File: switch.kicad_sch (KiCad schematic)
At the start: 2 parts, among them SW2 SW_Nidec_CAS-120A1

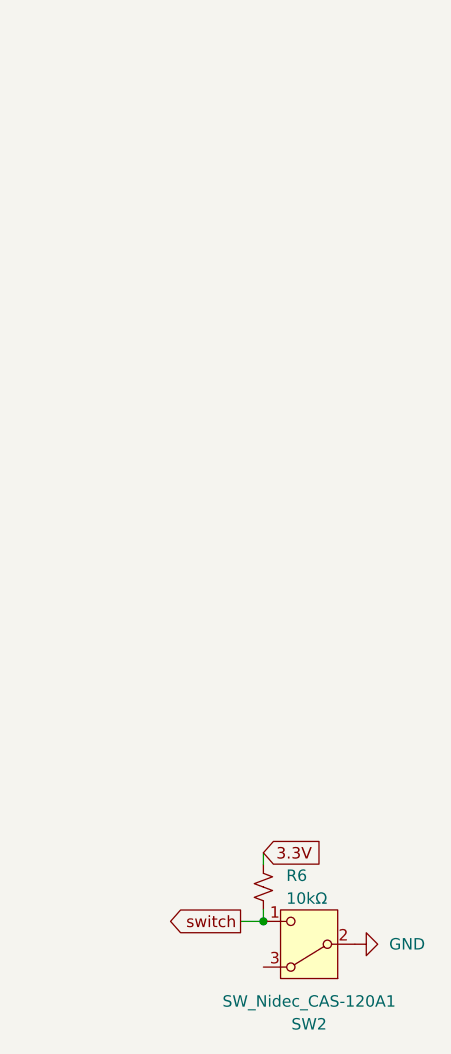
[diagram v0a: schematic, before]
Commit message: Overhaul
Overhauled the schematic so all the components are correct, rewired power to be 12 V instead of 9 V and connected hierarchical labels between modules. Added more decoupling capacitors where they were missing.
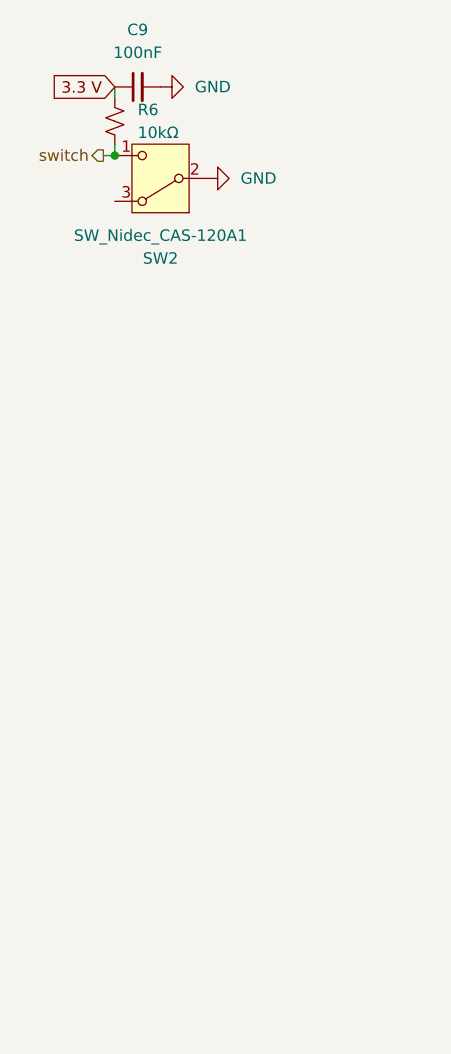
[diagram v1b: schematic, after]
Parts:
- added C9: 100nF, symbol Device:C_Small
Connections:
- net GND: now also C9.2
- net 3.3V renamed 3.3 V
- net 3.3 V: now also C9.1
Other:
- moved on the sheet: R6, SW2
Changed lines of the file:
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@@
 	(paper "A4")
 	(junction
-		(at 46.99 116.84)
+		(at 30.48 31.75)
 		(diameter 0)
 		(color 0 0 0 0)
@@
 	(wire
 		(pts
-			(xy 46.99 109.22) (xy 46.99 110.49)
+			(xy 30.48 24.13) (xy 30.48 25.4)
 		)
 		(stroke
@@
 	(wire
 		(pts
-			(xy 44.45 116.84) (xy 46.99 116.84)
+			(xy 29.21 31.75) (xy 30.48 31.75)
 		)
 		(stroke
@@
 	(wire
 		(pts
-			(xy 46.99 115.57) (xy 46.99 116.84)
+			(xy 30.48 30.48) (xy 30.48 31.75)
 		)
 		(stroke
@@
 		)
 	)
-	(global_label "switch"
-		(shape output)
-		(at 44.45 116.84 180)
+	(global_label "3.3 V"
+		(shape input)
+		(at 30.48 24.13 180)
 		(fields_autoplaced yes)
 		(effects
@@
 		)
 		(property "Intersheetrefs" "${INTERSHEET_REFS}"
-			(at 35.5381 116.84 0)
+			(at 22.4148 24.13 0)
 			(hide yes)
 			(show_name no)
@@
 		)
 	)
-	(global_label "3.3V"
-		(shape input)
-		(at 46.99 109.22 0)
-		(fields_autoplaced yes)
+	(hierarchical_label "switch"
+		(shape output)
+		(at 29.21 31.75 180)
 		(effects
 			(font
 				(size 1.27 1.27)
 			)
-			(justify left)
-		)
-		(property "Intersheetrefs" "${INTERSHEET_REFS}"
-			(at 54.0876 109.22 0)
-			(hide yes)
-			(show_name no)
-			(do_not_autoplace no)
-			(effects
-				(font
-					(size 1.27 1.27)
-				)
-				(justify left)
-			)
+			(justify right)
 		)
 	)
 	(symbol
 		(lib_id "Switch:SW_Nidec_CAS-120A1")
-		(at 52.07 119.38 180)
+		(at 35.56 34.29 180)
 		(unit 1)
 		(body_style 1)
@@
 		(fields_autoplaced yes)
 		(property "Reference" "SW2"
-			(at 52.07 128.27 0)
+			(at 35.56 43.18 0)
 			(show_name no)
 			(do_not_autoplace no)
@@
 		)
 		(property "Value" "SW_Nidec_CAS-120A1"
-			(at 52.07 125.73 0)
+			(at 35.56 40.64 0)
 			(show_name no)
 			(do_not_autoplace no)
@@
 		)
 		(property "Footprint" "Button_Switch_SMD:Nidec_Copal_CAS-120A"
-			(at 52.07 109.22 0)
+			(at 35.56 24.13 0)
 			(hide yes)
 			(show_name no)
@@
 		)
 		(property "Datasheet" "https://www.nidec-components.com/e/catalog/switch/cas.pdf"
-			(at 52.07 111.76 0)
+			(at 35.56 26.67 0)
 			(hide yes)
 			(show_name no)
@@
 		)
 		(property "Description" "Switch, single pole double throw"
-			(at 52.07 119.38 0)
+			(at 35.56 34.29 0)
 			(hide yes)
 			(show_name no)
@@
 	(symbol
 		(lib_id "power:GND")
-		(at 57.15 119.38 90)
+		(at 35.56 24.13 90)
 		(unit 1)
 		(body_style 1)
@@
 		(dnp no)
 		(fields_autoplaced yes)
-		(property "Reference" "#PWR014"
-			(at 63.5 119.38 0)
+		(property "Reference" "#PWR08"
+			(at 41.91 24.13 0)
 			(hide yes)
 			(show_name no)
@@
 		)
 		(property "Value" "GND"
-			(at 60.96 119.3799 90)
+			(at 39.37 24.1299 90)
 			(show_name no)
 			(do_not_autoplace no)
@@
 		)
 		(property "Footprint" ""
-			(at 57.15 119.38 0)
+			(at 35.56 24.13 0)
 			(hide yes)
 			(show_name no)
@@
 		)
 		(property "Datasheet" ""
-			(at 57.15 119.38 0)
+			(at 35.56 24.13 0)
 			(hide yes)
 			(show_name no)
@@
 		)
 		(property "Description" "Power symbol creates a global label with name \"GND\" , ground"
-			(at 57.15 119.38 0)
+			(at 35.56 24.13 0)
 			(hide yes)
 			(show_name no)
@@
 			(project "X19-Float-Board"
 				(path "/00000000-0000-0000-0000-000060e6118b/0ac88440-db6d-4d31-a4a6-0df1c7290ceb"
-					(reference "#PWR014")
+					(reference "#PWR08")
 					(unit 1)
 				)
@@
 	)
 	(symbol
-		(lib_id "Device:R_Small_US")
-		(at 46.99 113.03 180)
+		(lib_id "Device:C_Small")
+		(at 33.02 24.13 90)
 		(unit 1)
 		(body_style 1)
@@
 		(dnp no)
 		(fields_autoplaced yes)
+		(property "Reference" "C9"
+			(at 33.0263 17.78 90)
+			(show_name no)
+			(do_not_autoplace no)
+			(effects
+				(font
+					(size 1.27 1.27)
+				)
+			)
+		)
+		(property "Value" "100nF"
+			(at 33.0263 20.32 90)
+			(show_name no)
+			(do_not_autoplace no)
+			(effects
+				(font
+					(size 1.27 1.27)
+				)
+			)
+		)
+		(property "Footprint" ""
+			(at 33.02 24.13 0)
+			(hide yes)
+			(show_name no)
+			(do_not_autoplace no)
+			(effects
+				(font
+					(size 1.27 1.27)
+				)
+			)
+		)
+		(property "Datasheet" ""
+			(at 33.02 24.13 0)
+			(hide yes)
+			(show_name no)
+			(do_not_autoplace no)
+			(effects
+				(font
+					(size 1.27 1.27)
+				)
+			)
+		)
+		(property "Description" "Unpolarized capacitor, small symbol"
+			(at 33.02 24.13 0)
+			(hide yes)
+			(show_name no)
+			(do_not_autoplace no)
+			(effects
+				(font
+					(size 1.27 1.27)
+				)
+			)
+		)
+		(pin "1"
+		)
+		(pin "2"
+		)
+		(instances
+			(project "X19-Float-Board"
+				(path "/00000000-0000-0000-0000-000060e6118b/0ac88440-db6d-4d31-a4a6-0df1c7290ceb"
+					(reference "C9")
+					(unit 1)
+				)
+			)
+		)
+	)
+	(symbol
+		(lib_id "power:GND")
+		(at 40.64 34.29 90)
+		(unit 1)
+		(body_style 1)
+		(exclude_from_sim no)
+		(in_bom yes)
+		(on_board yes)
+		(in_pos_files yes)
+		(dnp no)
+		(fields_autoplaced yes)
+		(property "Reference" "#PWR014"
+			(at 46.99 34.29 0)
+			(hide yes)
+			(show_name no)
+			(do_not_autoplace no)
+			(effects
+				(font
+					(size 1.27 1.27)
+				)
+			)
+		)
+		(property "Value" "GND"
+			(at 44.45 34.2899 90)
+			(show_name no)
+			(do_not_autoplace no)
+			(effects
+				(font
+					(size 1.27 1.27)
+				)
+				(justify right)
+			)
+		)
+		(property "Footprint" ""
+			(at 40.64 34.29 0)
+			(hide yes)
+			(show_name no)
+			(do_not_autoplace no)
+			(effects
+				(font
+					(size 1.27 1.27)
+				)
+			)
+		)
+		(property "Datasheet" ""
+			(at 40.64 34.29 0)
+			(hide yes)
+			(show_name no)
+			(do_not_autoplace no)
+			(effects
+				(font
+					(size 1.27 1.27)
+				)
+			)
+		)
+		(property "Description" "Power symbol creates a global label with name \"GND\" , ground"
+			(at 40.64 34.29 0)
+			(hide yes)
+			(show_name no)
+			(do_not_autoplace no)
+			(effects
+				(font
+					(size 1.27 1.27)
+				)
+			)
+		)
+		(pin "1"
+		)
+		(instances
+			(project "X19-Float-Board"
+				(path "/00000000-0000-0000-0000-000060e6118b/0ac88440-db6d-4d31-a4a6-0df1c7290ceb"
+					(reference "#PWR014")
+					(unit 1)
+				)
+			)
+		)
+	)
+	(symbol
+		(lib_id "Device:R_Small_US")
+		(at 30.48 27.94 180)
+		(unit 1)
+		(body_style 1)
+		(exclude_from_sim no)
+		(in_bom yes)
+		(on_board yes)
+		(in_pos_files yes)
+		(dnp no)
+		(fields_autoplaced yes)
 		(property "Reference" "R6"
-			(at 49.53 111.7599 0)
+			(at 33.02 26.6699 0)
 			(show_name no)
 			(do_not_autoplace no)
@@
 		)
 		(property "Value" "10kΩ"
-			(at 49.53 114.2999 0)
+			(at 33.02 29.2099 0)
 			(show_name no)
 			(do_not_autoplace no)
@@
 		)
 		(property "Footprint" ""
-			(at 46.99 113.03 0)
+			(at 30.48 27.94 0)
 			(hide yes)
 			(show_name no)
@@
 		)
 		(property "Datasheet" ""
-			(at 46.99 113.03 0)
+			(at 30.48 27.94 0)
 			(hide yes)
 			(show_name no)
@@
 		)
 		(property "Description" "Resistor, small US symbol"
-			(at 46.99 113.03 0)
-			(hide yes)
-			(show_name no)
+			(at 30.48 27.94 0)
+			(hide yes)
+			(show_name no)

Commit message: Gave footprints to everything
Footprints
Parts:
- C9: footprint (none) -> Capacitor_SMD:C_0603_1608Metric
- R6: footprint (none) -> Resistor_SMD:R_0603_1608Metric
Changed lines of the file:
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@@
 			)
 		)
-		(property "Footprint" ""
+		(property "Footprint" "Capacitor_SMD:C_0603_1608Metric"
 			(at 33.02 24.13 0)
 			(hide yes)
@@
 			)
 		)
-		(property "Footprint" ""
+		(property "Footprint" "Resistor_SMD:R_0603_1608Metric"
 			(at 30.48 27.94 0)
 			(hide yes)

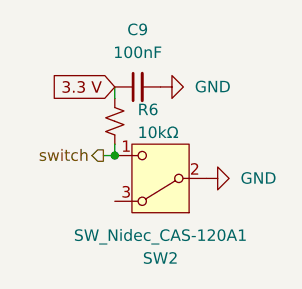
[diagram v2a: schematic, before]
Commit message: USB-C + Complete wiring
Compltetly wired the pcb (I don't understand the DRC errors) and added a usb C to flash the stm, modified the switch to be the BOOT0 for the stm so it controls whether the stm is in flash mode
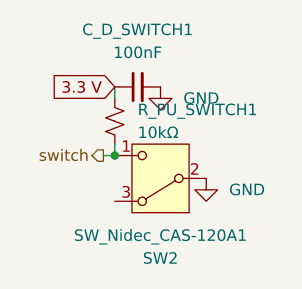
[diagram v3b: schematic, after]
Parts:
- renumbered C9 to C_D_SWITCH1, R6 to R_PU_SWITCH1
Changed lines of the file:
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@@
 	(symbol
 		(lib_id "power:GND")
-		(at 35.56 24.13 90)
+		(at 35.56 24.13 0)
 		(unit 1)
 		(body_style 1)
@@
 		(fields_autoplaced yes)
 		(property "Reference" "#PWR08"
-			(at 41.91 24.13 0)
+			(at 35.56 30.48 0)
 			(hide yes)
 			(show_name no)
@@
 		)
 		(property "Value" "GND"
-			(at 39.37 24.1299 90)
-			(show_name no)
-			(do_not_autoplace no)
-			(effects
-				(font
-					(size 1.27 1.27)
-				)
-				(justify right)
+			(at 38.1 25.3999 0)
+			(show_name no)
+			(do_not_autoplace no)
+			(effects
+				(font
+					(size 1.27 1.27)
+				)
+				(justify left)
 			)
 		)
@@
 		(dnp no)
 		(fields_autoplaced yes)
-		(property "Reference" "C9"
+		(property "Reference" "C_D_SWITCH1"
 			(at 33.0263 17.78 90)
 			(show_name no)
@@
 			(project "X19-Float-Board"
 				(path "/00000000-0000-0000-0000-000060e6118b/0ac88440-db6d-4d31-a4a6-0df1c7290ceb"
-					(reference "C9")
+					(reference "C_D_SWITCH1")
 					(unit 1)
 				)
@@
 	(symbol
 		(lib_id "power:GND")
-		(at 40.64 34.29 90)
+		(at 40.64 34.29 0)
 		(unit 1)
 		(body_style 1)
@@
 		(fields_autoplaced yes)
 		(property "Reference" "#PWR014"
-			(at 46.99 34.29 0)
+			(at 40.64 40.64 0)
 			(hide yes)
 			(show_name no)
@@
 		)
 		(property "Value" "GND"
-			(at 44.45 34.2899 90)
-			(show_name no)
-			(do_not_autoplace no)
-			(effects
-				(font
-					(size 1.27 1.27)
-				)
-				(justify right)
+			(at 43.18 35.5599 0)
+			(show_name no)
+			(do_not_autoplace no)
+			(effects
+				(font
+					(size 1.27 1.27)
+				)
+				(justify left)
 			)
 		)
@@
 		(dnp no)
 		(fields_autoplaced yes)
-		(property "Reference" "R6"
+		(property "Reference" "R_PU_SWITCH1"
 			(at 33.02 26.6699 0)
 			(show_name no)
@@
 			(project "X19-Float-Board"
 				(path "/00000000-0000-0000-0000-000060e6118b/0ac88440-db6d-4d31-a4a6-0df1c7290ceb"
-					(reference "R6")
+					(reference "R_PU_SWITCH1")
 					(unit 1)
 				)

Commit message: Updated Schematic
Updated parts of todo list for schematic
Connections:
- no-connect marks 0 -> 1
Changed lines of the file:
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@@
 		(color 0 0 0 0)
+	)
+	(no_connect
+		(at 30.48 36.83)
 	)
 	(wire

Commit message: USB, TVS, LDO, Passives, I2C
applied changes to usb circuitry, tvs, ldo, passibes and i2c.
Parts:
- removed C_D_SWITCH1: 100nF, Capacitor_SMD:C_0603_1608Metric, symbol Device:C_Small
- removed R_PU_SWITCH1: 10kΩ, Resistor_SMD:R_0603_1608Metric, symbol Device:R_Small_US
- removed SW2: SW_Nidec_CAS-120A1, Button_Switch_SMD:Nidec_Copal_CAS-120A, symbol Switch:SW_Nidec_CAS-120A1
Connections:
- no-connect marks 1 -> 0
